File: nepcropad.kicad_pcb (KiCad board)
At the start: 2 copper layers, 58.7 x 65.2 mm, 37 parts, among them J1 USB_C_Receptacle_USB2.0, SW1 SW_Push, U1 ATmega32U4-A, Y1 16MHz

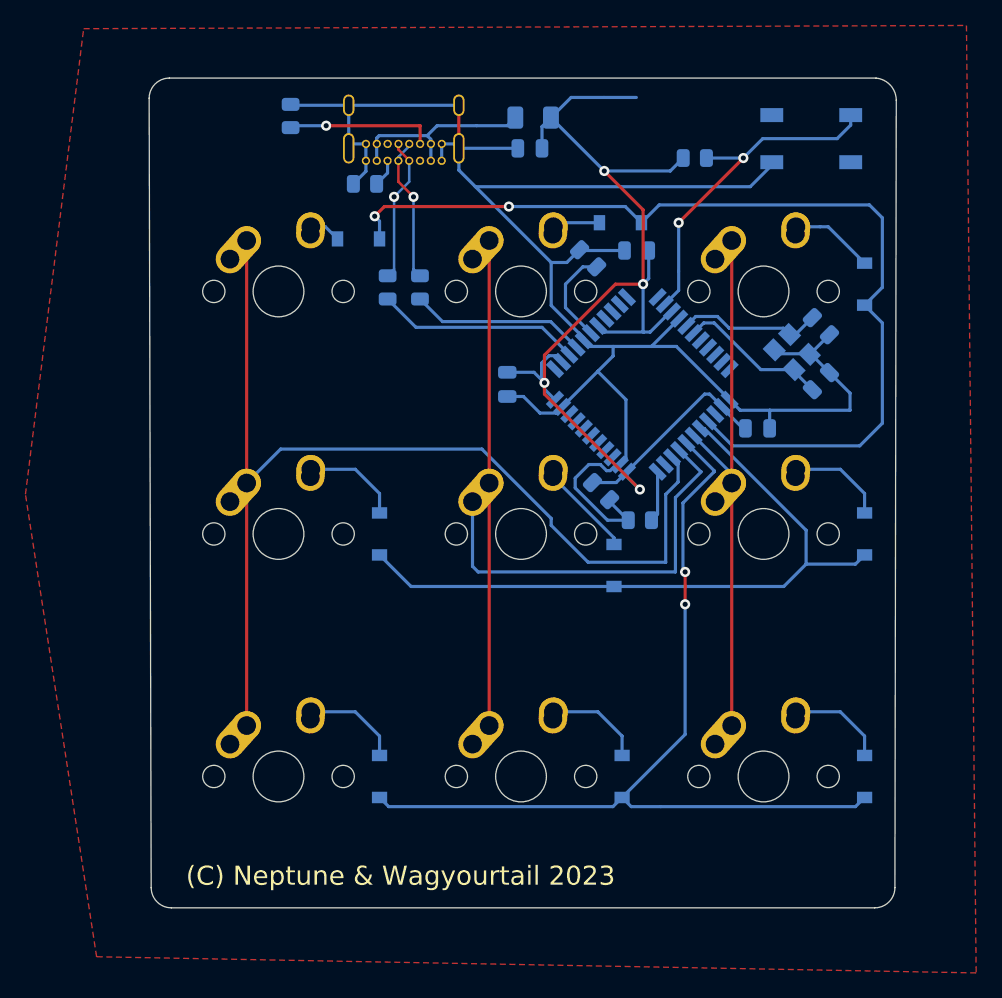
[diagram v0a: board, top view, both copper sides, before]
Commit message: Should be ready for placing an order
Added CPL and BOM

Changed out the USB-C connector as the original one we used is nolonger in production.
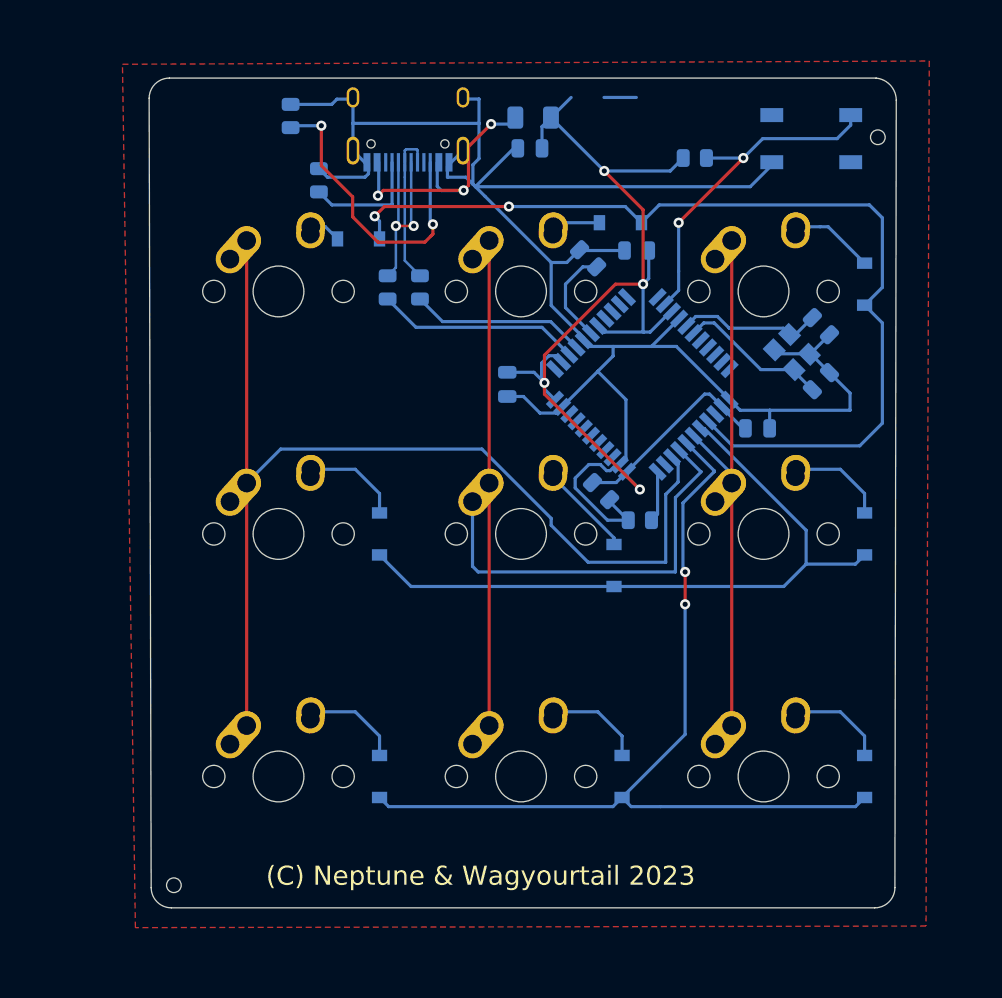
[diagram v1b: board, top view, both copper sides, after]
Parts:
- J1: footprint usbc:USB_C_GCT_USB4085 -> jlcusbc:TYPE-C-31-M-12
- moved R5 3.63 mm to (138.1, 62.7), turned to 90 degrees
- moved J1 1.17 mm to (145.1, 56.2)
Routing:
- net Net-(J1-PadB5): track 11.7 -> 23.8 mm, vias 1 -> 2
- net GND: track 153.1 -> 160.8 mm
- net Net-(J1-PadA5): track 2.17 -> 9.56 mm
- net VCC: track 15.4 -> 22.1 mm, vias 0 -> 3
- net D-: track 11.4 -> 15.7 mm, vias 1 -> 2
- net +5V: track 95.8 -> 93.3 mm
- net D+: track 11.4 -> 12.1 mm, vias 1 -> 0
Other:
- outline, holes or cut-outs redrawn

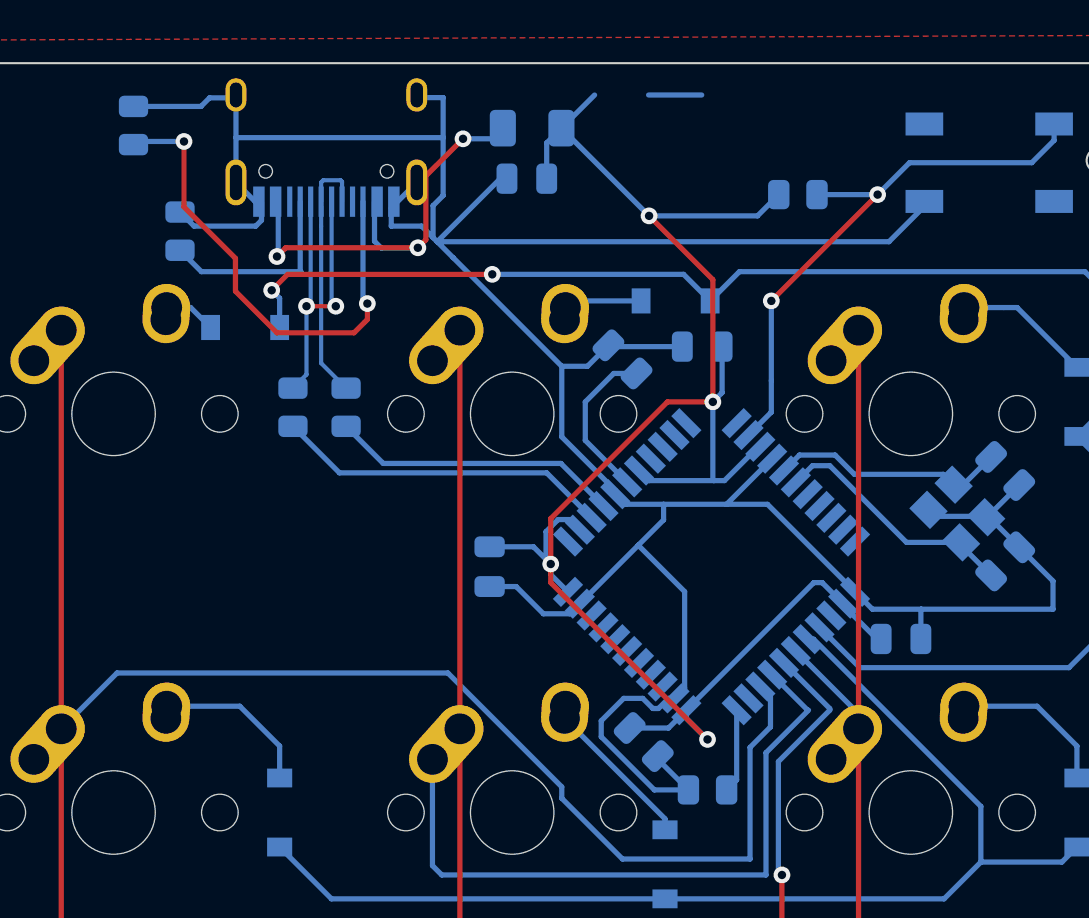
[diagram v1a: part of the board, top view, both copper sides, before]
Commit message: MCU Footprint wrong for new MCU
I was about to checkout and noticed on the manufacturer's site that the MCU was a different size than the footprint used.

ATmega32U4-MUR smaller than AU version
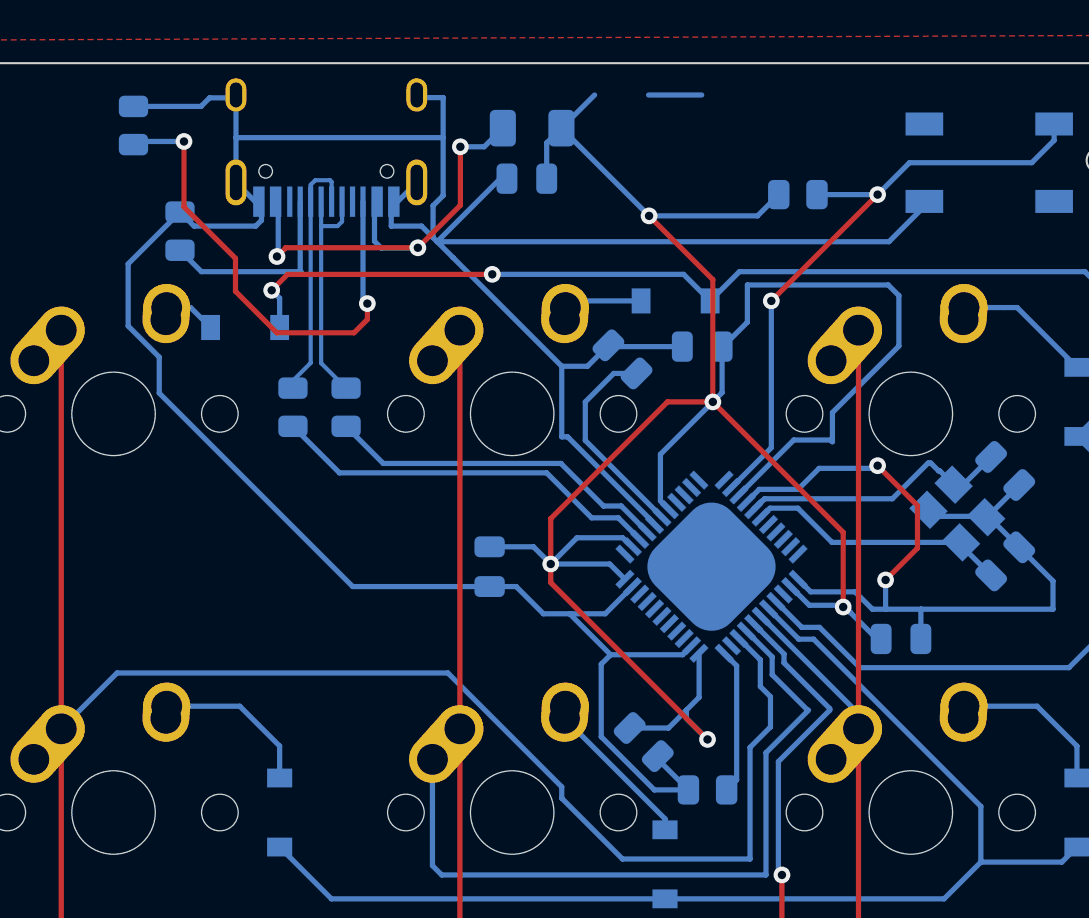
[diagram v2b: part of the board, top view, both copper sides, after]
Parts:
- U1: footprint Package_QFP:TQFP-44_10x10mm_P0.8mm -> ATmega32U4-MU:QFN44G-0.5-7X7MM
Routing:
- net +5V: track 93.3 -> 125.3 mm, vias 4 -> 5
- net GND: track 160.8 -> 188.5 mm, vias 0 -> 2
- net D-: track 15.7 -> 12.1 mm, vias 2 -> 0
- net Net-(R4-Pad2): track 4.01 -> 6.99 mm
- net Net-(R1-Pad2): track 27.2 -> 30.1 mm
- net COL0: track 85.0 -> 87.7 mm
- net COL1: track 70.4 -> 73.0 mm
- net ROW0: track 76.2 -> 78.8 mm
- net ROW2: track 71.2 -> 73.7 mm
- net ROW1: track 54.4 -> 56.9 mm
- net Net-(C2-Pad2): track 11.3 -> 13.8 mm
- net Net-(R3-Pad2): track 16.1 -> 18.5 mm
- net COL2: track 43.1 -> 45.4 mm
- net Net-(C3-Pad1): track 7.69 -> 10.0 mm
- net Net-(R2-Pad2): track 13.9 -> 16.2 mm
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
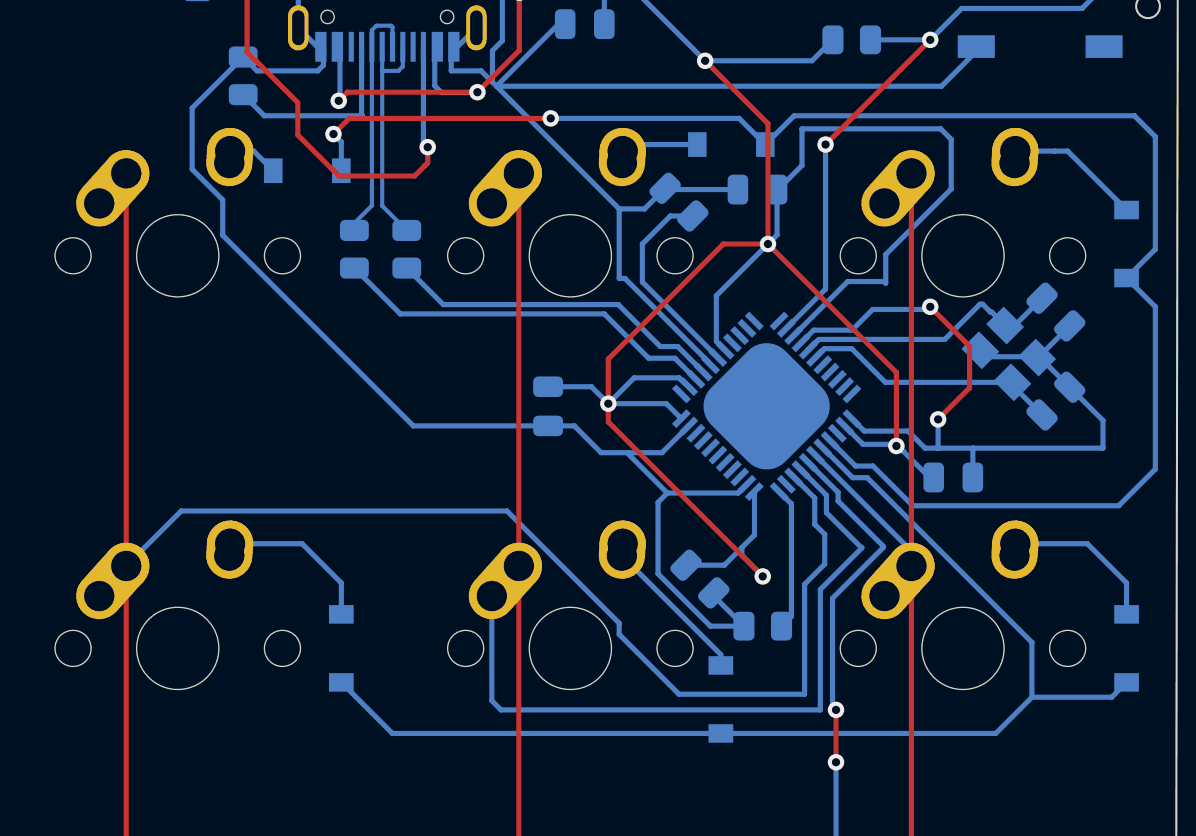
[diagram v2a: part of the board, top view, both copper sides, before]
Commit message: Just a quick fix
Added gerbers for new version as well
Cleaned up some routing for the gnd traces
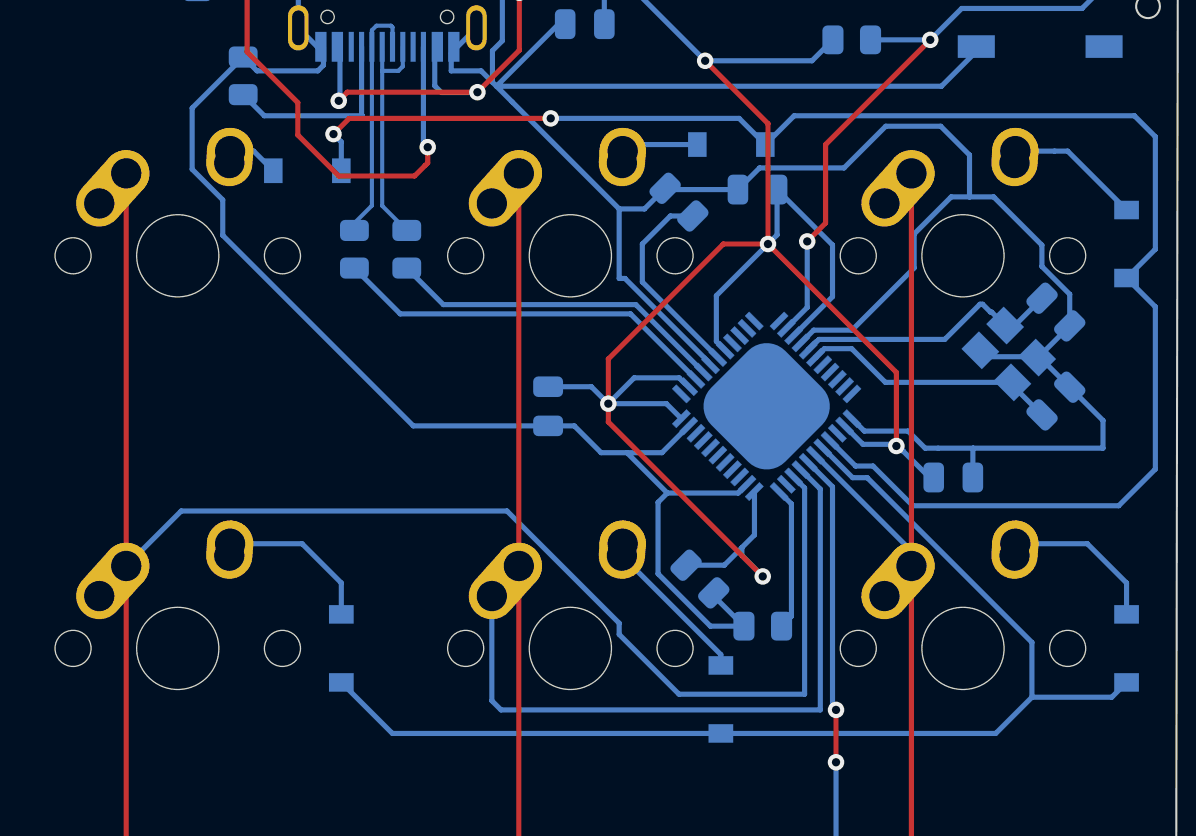
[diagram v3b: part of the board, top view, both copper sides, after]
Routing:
- net GND: track 188.5 -> 209.4 mm, vias 2 -> 0
- net +5V: track 125.3 -> 109.6 mm
- net ROW2: track 73.7 -> 71.6 mm
- net COL1: track 73.0 -> 71.3 mm
- net COL0: track 87.7 -> 86.9 mm

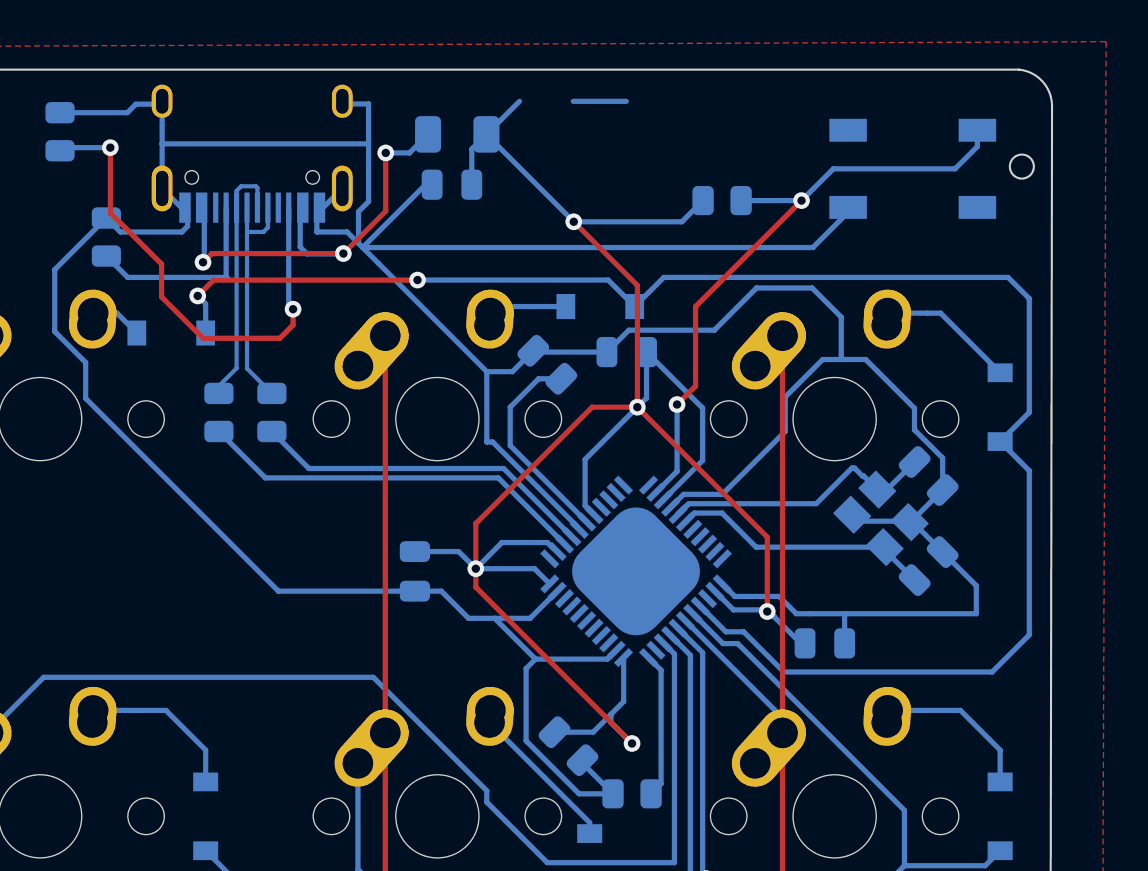
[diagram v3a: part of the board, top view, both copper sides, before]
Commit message: More routing cleanup
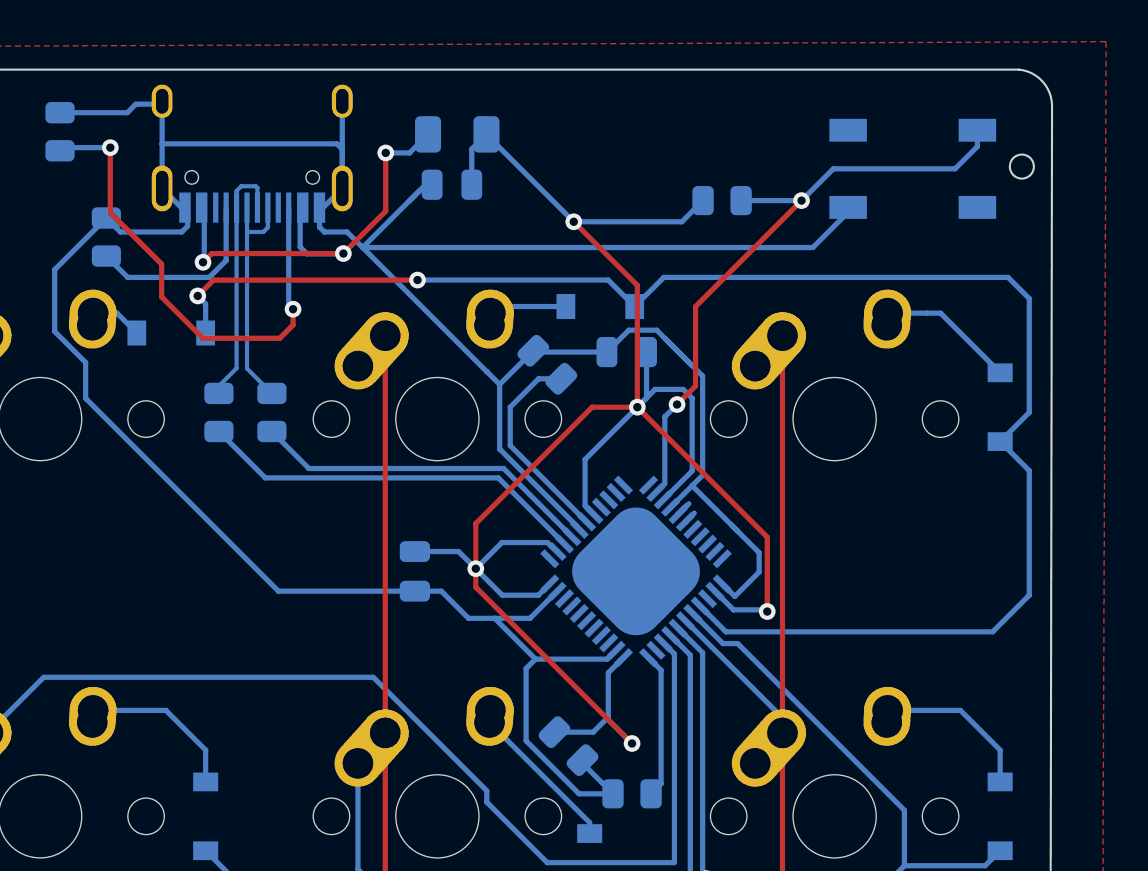
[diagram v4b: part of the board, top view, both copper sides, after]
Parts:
- removed C1, C2: 22pF, Capacitor_SMD:C_0805_2012Metric
- removed C4: 0.1uF, Capacitor_SMD:C_0805_2012Metric
- removed Y1: 16MHz, Crystal:Crystal_SMD_3225-4Pin_3.2x2.5mm
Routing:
- net GND: track 209.4 -> 168.3 mm
- net Net-(C2-Pad2): track 13.8 -> 1.31 mm
- net Net-(C1-Pad2): track 12.6 -> 0.64 mm
- net +5V: track 109.6 -> 102.3 mm
- net ROW0: track 78.8 -> 76.1 mm
- net Net-(J1-PadA5): track 9.56 -> 9.04 mm
